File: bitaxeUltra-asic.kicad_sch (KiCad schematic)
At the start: 16 parts, among them J1 54-00164

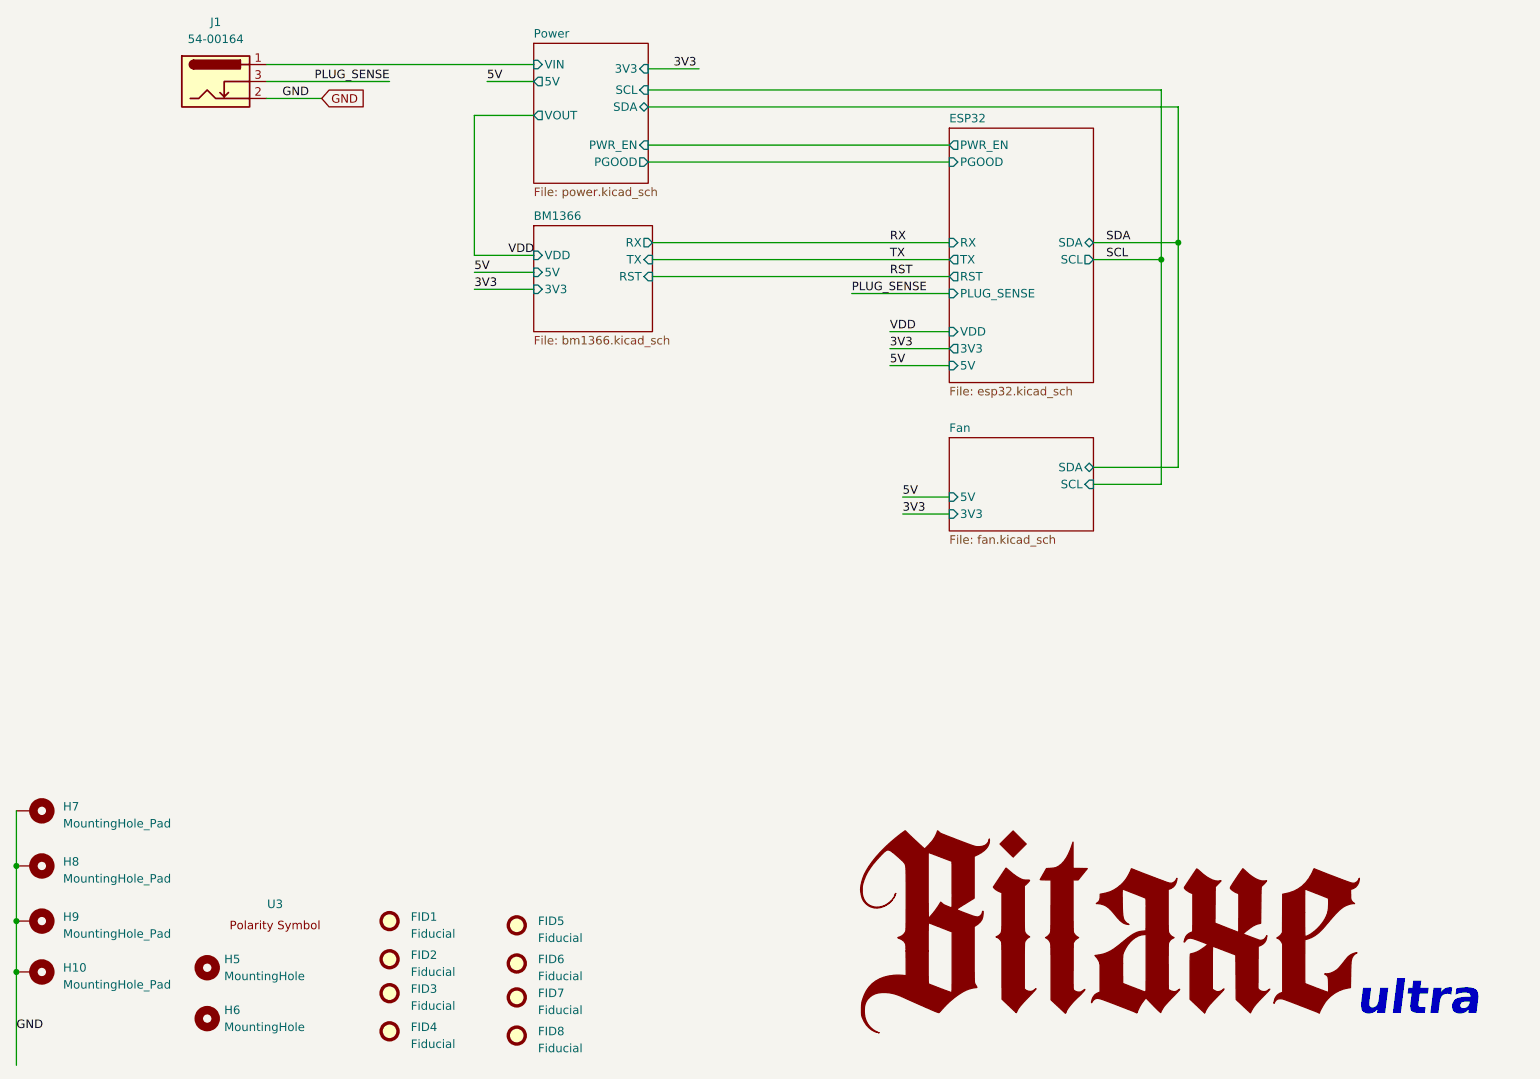
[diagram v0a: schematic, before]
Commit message: routing for ASIC board
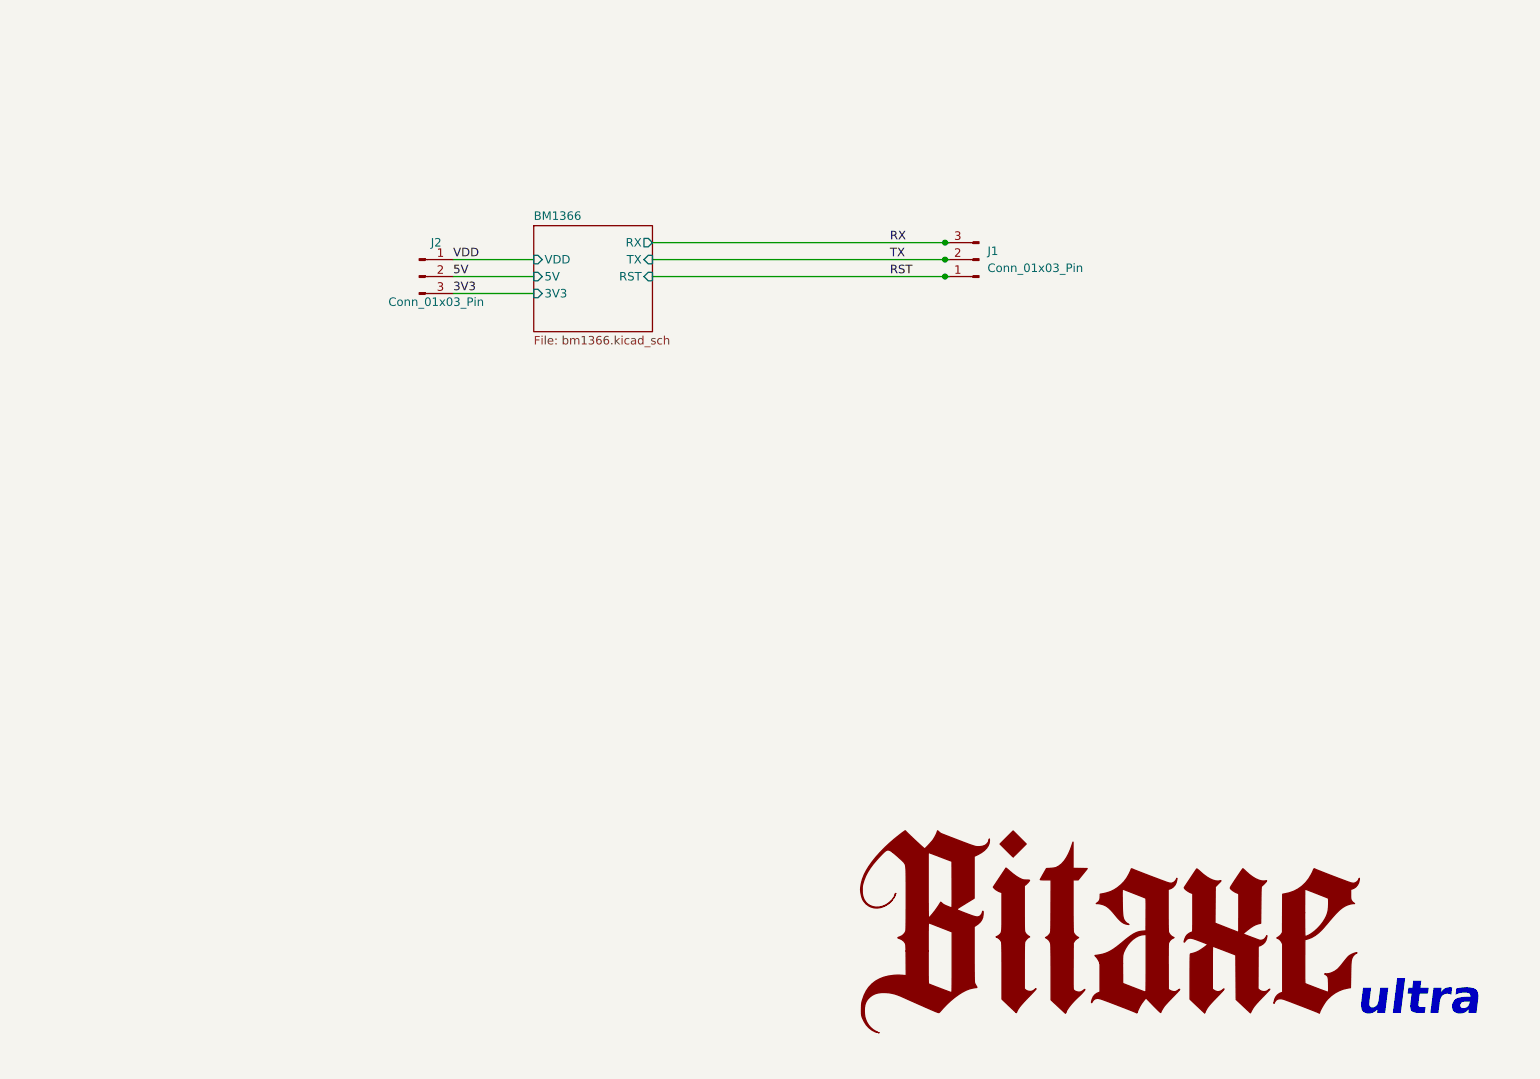
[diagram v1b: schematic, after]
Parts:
- removed FID1, FID2, FID3, FID4, FID5, FID6, FID7, FID8: Fiducial, Fiducial:Fiducial_1mm_Mask2mm, symbol Mechanical:Fiducial
- removed H10, H7, H8, H9: MountingHole_Pad, MountingHole:MountingHole_3mm_Pad_Via, symbol Mechanical:MountingHole_Pad
- removed H5, H6: MountingHole, MountingHole:MountingHole_3.5mm, symbol Mechanical:MountingHole
- removed J1: 54-00164, bitaxe:BarrelJack_Wuerth_694106106102_2.0x5.5mm, symbol Connector:Barrel_Jack_Switch
- removed U3: ~, bitaxe:polarity, symbol bitaxe:polarity
- added J1: Conn_01x03_Pin, Connector_JST:JST_PH_B3B-PH-K_1x03_P2.00mm_Vertical, symbol Connector:Conn_01x03_Pin
- added J2: Conn_01x03_Pin, Connector_Wire:SolderWire-0.5sqmm_1x03_P4.8mm_D0.9mm_OD2.3mm_Relief, symbol Connector:Conn_01x03_Pin
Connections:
- net 3V3: now also J2.3 (Pin_3)
- net 5V: now also J2.2 (Pin_2)
- net RST: now also J1.1 (Pin_1)
- net RX: now also J1.3 (Pin_3)
- net TX: now also J1.2 (Pin_2)
- net VDD: now also J2.1 (Pin_1)
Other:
- removed sheet ESP32
- removed sheet Fan
- removed sheet Power
